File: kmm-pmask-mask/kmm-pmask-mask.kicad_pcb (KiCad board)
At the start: 4 copper layers, 90.4 x 109 mm, 68 parts, among them J1 F31L-1A7H1-11030, U1 MS5611-01BA, U10 MAX30101EFD_T, U11 SHT40-AD1B-R3, U12 SHT40-AD1B-R3, U13 TMP117MAIDRVR, U14 TMP117MAIDRVR, U15 TCA9546APW, U2 MAX30101EFD_T, U3 SHT40-AD1B-R3, U4 TMP117MAIDRVR, U5 MS5611-01BA, U6 MS5611-01BA, U7 MS5611-01BA, U8 MAX30101EFD_T, U9 MAX30101EFD_T

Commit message: initial routing
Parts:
- moved C1 6.00 mm to (77.4, 69.2)
- moved C17 5.65 mm to (84.6, 142.8), turned to 90 degrees
- moved R8 4.84 mm to (81.0, 58.8), turned to 90 degrees
- moved R1 4.80 mm to (69.2, 58.8), turned to 90 degrees
- moved C26 3.60 mm to (93.2, 143.0), turned to -90 degrees
- moved C19 3.41 mm to (78.6, 140.9), turned to 90 degrees
- moved R2 3.33 mm to (71.2, 58.8)
- moved C11 3.20 mm to (93.4, 82.4), turned to 180 degrees
- moved C13 3.20 mm to (49.4, 96.6), turned to 0 degrees
- moved C21 2.61 mm to (61.4, 78.8), turned to 0 degrees
- moved C6 2.60 mm to (74.4, 73.6), turned to 180 degrees
- moved C8 2.60 mm to (77.0, 73.6), turned to 0 degrees
- moved C24 2.58 mm to (42.0, 110.8), turned to 0 degrees
- moved C2 2.28 mm to (54.2, 82.8), turned to 0 degrees
- moved C20 2.28 mm to (83.6, 143.0), turned to 90 degrees
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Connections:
- C10 pad 1: +5V -> +1.8V
- C12 pad 1: +1.8V -> +5V
- C14 pad 1: +5V -> +1.8V
- C16 pad 1: +1.8V -> +5V
- C18 pad 1: +5V -> +1.8V
- C20 pad 1: +1.8V -> +5V
- C5 pad 1: +1.8V -> +5V
- C7 pad 1: +5V -> +1.8V
- J1 pad 1: unconnected-(J1-Pin_1-Pad1) -> +5V
- J1 pad 11: unconnected-(J1-Pin_11-Pad11) -> /~{I2C_M_RST}
- J1 pad 12: unconnected-(J1-Pin_12-Pad12) -> GND
- J1 pad 13: unconnected-(J1-Pin_13-Pad13) -> /I2C_M_SDA
- J1 pad 14: unconnected-(J1-Pin_14-Pad14) -> /I2C_M_SCL
- J1 pad 15: unconnected-(J1-Pin_15-Pad15) -> GND
- J1 pad 16: unconnected-(J1-Pin_16-Pad16) -> GND
- J1 pad 17: unconnected-(J1-Pin_17-Pad17) -> /I2C_M_SCL
- J1 pad 18: unconnected-(J1-Pin_18-Pad18) -> /I2C_M_SDA
- J1 pad 19: unconnected-(J1-Pin_19-Pad19) -> GND
- J1 pad 2: unconnected-(J1-Pin_2-Pad2) -> +5V
- J1 pad 20: unconnected-(J1-Pin_20-Pad20) -> /~{I2C_M_RST}
- J1 pad 23: unconnected-(J1-Pin_23-Pad23) -> GND
- J1 pad 24: unconnected-(J1-Pin_24-Pad24) -> +1.8V
- J1 pad 25: unconnected-(J1-Pin_25-Pad25) -> GND
- J1 pad 26: unconnected-(J1-Pin_26-Pad26) -> +3.3V
- J1 pad 27: unconnected-(J1-Pin_27-Pad27) -> +3.3V
- J1 pad 28: unconnected-(J1-Pin_28-Pad28) -> GND
- J1 pad 29: unconnected-(J1-Pin_29-Pad29) -> +5V
- J1 pad 3: unconnected-(J1-Pin_3-Pad3) -> GND
- J1 pad 30: unconnected-(J1-Pin_30-Pad30) -> +5V
- J1 pad 4: unconnected-(J1-Pin_4-Pad4) -> +3.3V
- J1 pad 5: unconnected-(J1-Pin_5-Pad5) -> +3.3V
- J1 pad 6: unconnected-(J1-Pin_6-Pad6) -> GND
- J1 pad 7: unconnected-(J1-Pin_7-Pad7) -> +1.8V
- J1 pad 8: unconnected-(J1-Pin_8-Pad8) -> GND
- U1 pad 7: /I2C0_SDA -> /I2C1_SDA
- U1 pad 8: /I2C0_SCL -> /I2C1_SCL
- U10 pad 10: +1.8V -> +5V
- U10 pad 11: +5V -> +1.8V
- U10 pad 2: /I2C3_SCL -> /I2C2_SCL
- U10 pad 3: /I2C3_SDA -> /I2C2_SDA
- U10 pad 9: +1.8V -> +5V
- U11 pad 1: /I2C1_SDA -> /I2C0_SDA
- U11 pad 2: /I2C1_SCL -> /I2C0_SCL
- U12 pad 1: /I2C1_SDA -> /I2C2_SDA
- U12 pad 2: /I2C1_SCL -> /I2C2_SCL
- U13 pad 1: /I2C2_SCL -> /I2C3_SCL
- U13 pad 6: /I2C2_SDA -> /I2C3_SDA
- U14 pad 1: /I2C3_SCL -> /I2C2_SCL
- U14 pad 6: /I2C3_SDA -> /I2C2_SDA
- U2 pad 10: +1.8V -> +5V
- U2 pad 11: +5V -> +1.8V
- U2 pad 2: /I2C0_SCL -> /I2C1_SCL
- U2 pad 3: /I2C0_SDA -> /I2C1_SDA
- U2 pad 9: +1.8V -> +5V
- U3 pad 1: /I2C1_SDA -> /I2C3_SDA
- U3 pad 2: /I2C1_SCL -> /I2C3_SCL
- U4 pad 1: /I2C1_SCL -> /I2C0_SCL
- U4 pad 6: /I2C1_SDA -> /I2C0_SDA
- U5 pad 7: /I2C1_SDA -> /I2C0_SDA
- U5 pad 8: /I2C1_SCL -> /I2C0_SCL
- U6 pad 7: /I2C2_SDA -> /I2C3_SDA
- U6 pad 8: /I2C2_SCL -> /I2C3_SCL
- U7 pad 7: /I2C3_SDA -> /I2C2_SDA
- U7 pad 8: /I2C3_SCL -> /I2C2_SCL
- U8 pad 10: +1.8V -> +5V
- U8 pad 11: +5V -> +1.8V
- U8 pad 2: /I2C2_SCL -> /I2C3_SCL
- U8 pad 3: /I2C2_SDA -> /I2C3_SDA
- U8 pad 9: +1.8V -> +5V
- U9 pad 10: +1.8V -> +5V
- U9 pad 11: +5V -> +1.8V
- U9 pad 2: /I2C1_SCL -> /I2C0_SCL
- U9 pad 3: /I2C1_SDA -> /I2C0_SDA
- U9 pad 9: +1.8V -> +5V
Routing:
- net +3.3V: track 0.00 -> 345.1 mm, vias 0 -> 19
- net +5V: track 0.00 -> 260.6 mm, vias 0 -> 7
- net +1.8V: track 0.00 -> 243.6 mm, vias 0 -> 7
- net /I2C2_SDA: track 0.00 -> 155.5 mm
- net /I2C2_SCL: track 0.00 -> 154.8 mm, vias 0 -> 2
- net /I2C0_SDA: track 0.00 -> 80.2 mm, vias 0 -> 2
- net /I2C0_SCL: track 0.00 -> 74.4 mm, vias 0 -> 2
- net /I2C3_SCL: track 0.00 -> 73.0 mm, vias 0 -> 2
- net /I2C3_SDA: track 0.00 -> 72.5 mm, vias 0 -> 2
- net GND: track 0.00 -> 55.9 mm, vias 0 -> 63
- net /I2C1_SDA: track 0.00 -> 29.4 mm
- net /I2C1_SCL: track 0.00 -> 27.8 mm
- net /~{I2C_M_RST}: track 0.00 -> 15.0 mm, vias 0 -> 2
- net /I2C_M_SDA: track 0.00 -> 10.8 mm
- net /I2C_M_SCL: track 0.00 -> 9.21 mm
- added copper zone on F.Cu, net +3.3V
- added copper zone on F.Cu, net +5V
- added copper zone on B.Cu, net GND
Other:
- outline, holes or cut-outs redrawn
- board text added: "STIFFENER PI (Polyamide) 0.2mm"
- board text removed: "STIFFENER FR-4 0.2mm"

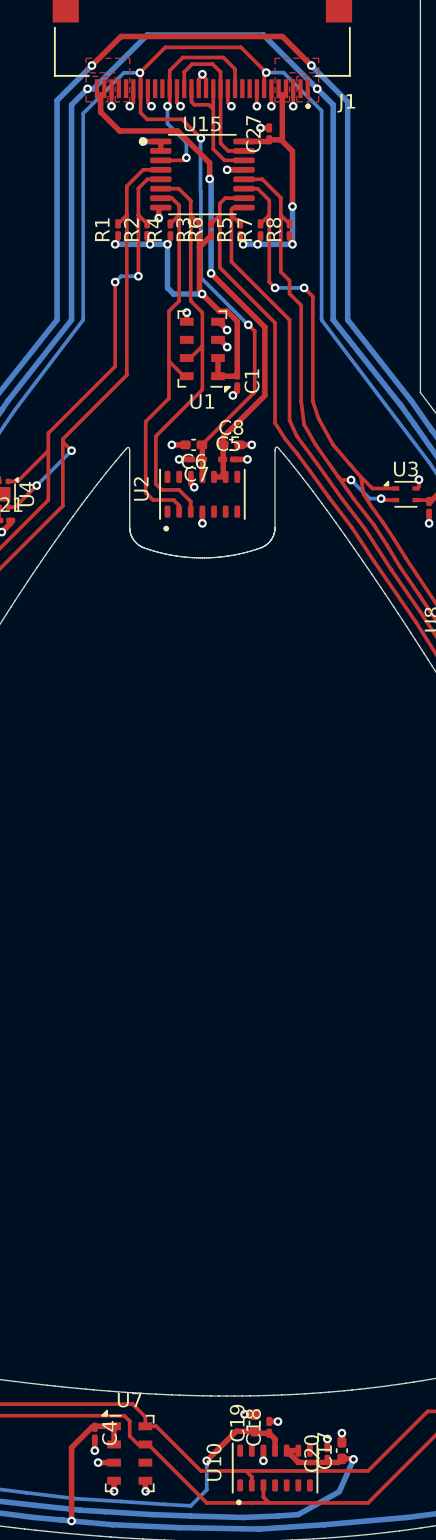
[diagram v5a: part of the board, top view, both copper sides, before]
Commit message: Schematic annotations, power flags
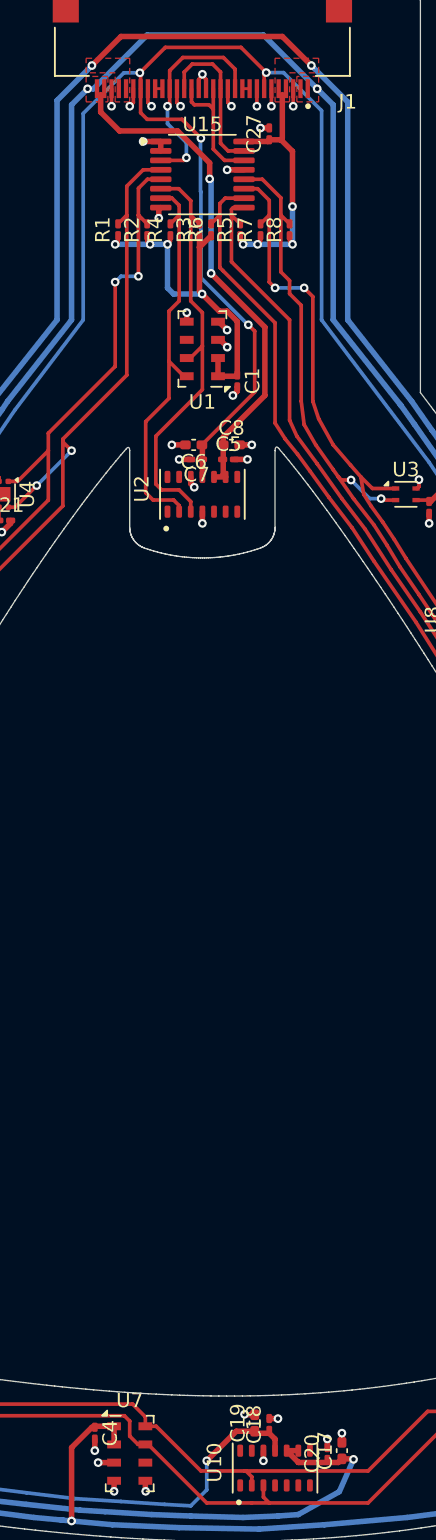
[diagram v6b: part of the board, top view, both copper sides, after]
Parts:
- moved C18 0.20 mm to (79.6, 141.0)
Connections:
- J1 pad 10: unconnected-(J1-Pin_10-Pad10) -> Net-(J1-Pin_10)
- J1 pad 21: unconnected-(J1-Pin_21-Pad21) -> Net-(J1-Pin_21)
- J1 pad 22: unconnected-(J1-Pin_22-Pad22) -> Net-(J1-Pin_21)
- J1 pad 9: unconnected-(J1-Pin_9-Pad9) -> Net-(J1-Pin_10)
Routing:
- net Net-(J1-Pin_21): track 0.00 -> 0.50 mm
- net Net-(J1-Pin_10): track 0.00 -> 0.50 mm

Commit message: change stackup to 2 layers
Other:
- copper layers 4 -> 2
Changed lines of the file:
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@@
 	(generator_version "10.0")
 	(general
-		(thickness 0.1905)
+		(thickness 0.115)
 		(legacy_teardrops no)
 	)
@@
 	(layers
 		(0 "F.Cu" signal)
-		(4 "In1.Cu" signal)
-		(6 "In2.Cu" signal)
 		(2 "B.Cu" signal)
 		(13 "F.Paste" user)
@@
 			(layer "F.Cu"
 				(type "copper")
-				(thickness 0.012)
+				(thickness 0.0175)
 			)
 			(layer "dielectric 1"
 				(type "core")
 				(color "Polyimide")
-				(thickness 0.0125 locked)
-				(material "Polyimide")
-				(epsilon_r 3.2)
-				(loss_tangent 0.004) addsublayer
 				(thickness 0.025 locked)
-			)
-			(layer "In1.Cu"
-				(type "copper")
-				(thickness 0.012)
-			)
-			(layer "dielectric 2"
-				(type "core")
-				(color "Polyimide")
-				(thickness 0.0125 locked)
 				(material "Polyimide")
 				(epsilon_r 3.2)
 				(loss_tangent 0.004)
 			)
-			(layer "In2.Cu"
-				(type "copper")
-				(thickness 0.012)
-			)
-			(layer "dielectric 3"
-				(type "core")
-				(color "Polyimide")
-				(thickness 0.0125 locked)
-				(material "Polyimide")
-				(epsilon_r 3.2)
-				(loss_tangent 0.004) addsublayer
-				(thickness 0.025 locked)
-			)
 			(layer "B.Cu"
 				(type "copper")
-				(thickness 0.012)
+				(thickness 0.0175)
 			)
 			(layer "B.Mask"
